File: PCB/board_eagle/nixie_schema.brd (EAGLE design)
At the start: 150 x 170 mm, 103 parts, among them P1 100k, Q1 BC856B, Q2 IRF740S, U2 MC7940N

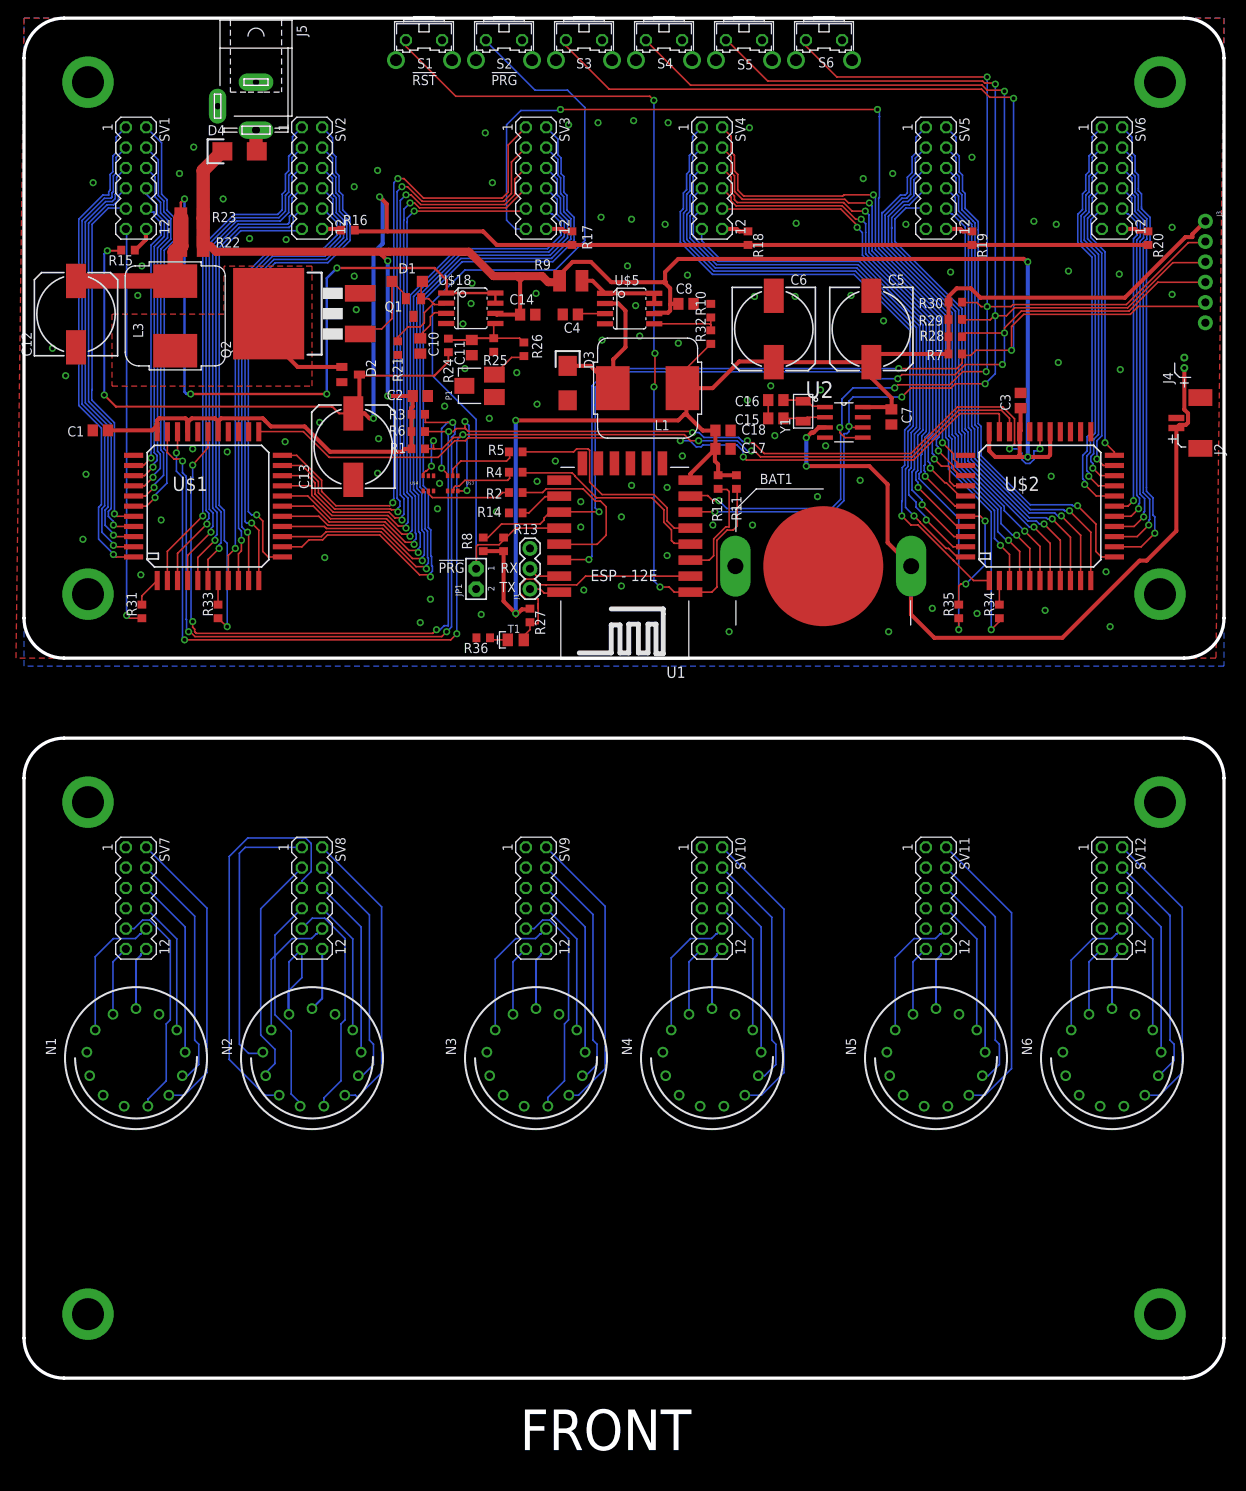
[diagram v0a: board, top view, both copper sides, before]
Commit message: Started fixing nixie tube footprint
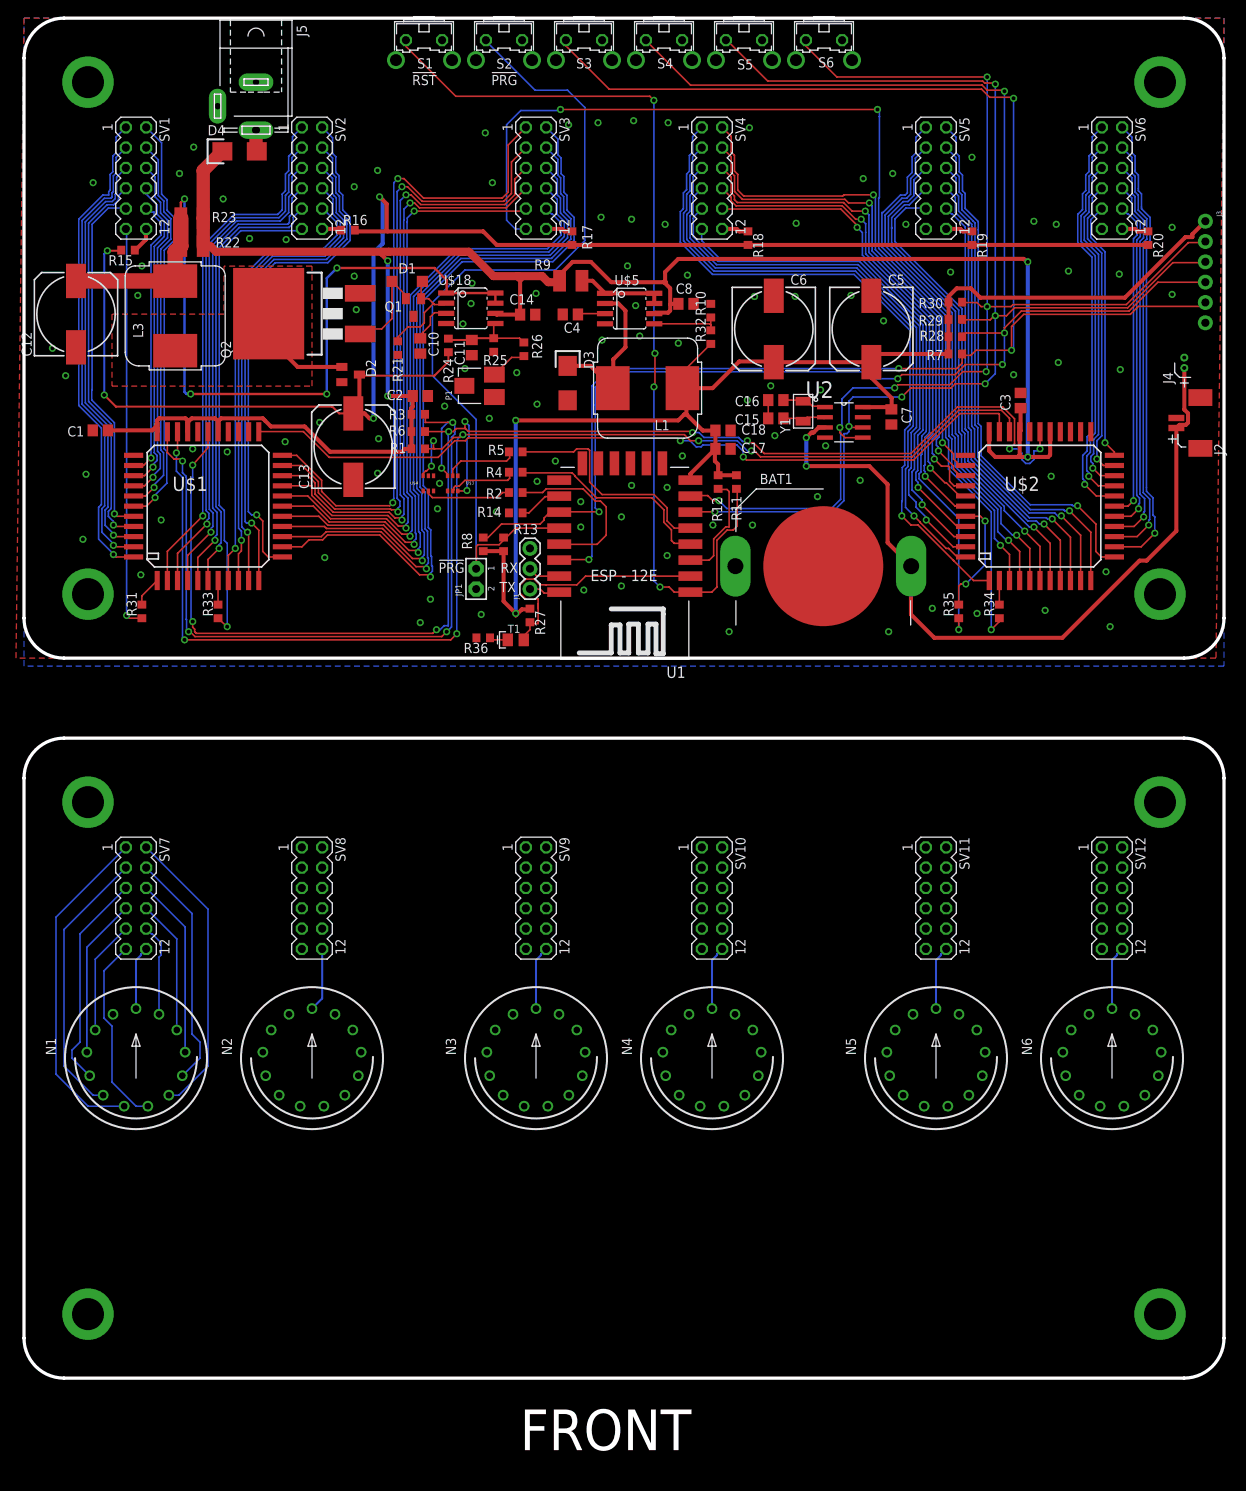
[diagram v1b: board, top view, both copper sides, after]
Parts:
- N1, N2, N3, N4, N5, N6: value IN-14 -> IN-14_FIXED
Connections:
- removed net N$101: N3.LHDP, SV9.11
- removed net N$102: N4.LHDP, SV10.11
- removed net N$104: N6.LHDP, SV12.11
- removed net N$105: N5.LHDP, SV11.11
- removed net N$31: N1.7, SV7.5
- removed net N$32: N1.8, SV7.3
- removed net N$33: N1.9, SV7.1
- removed net N$34: N2.9, SV8.1
- removed net N$35: N2.0, SV8.10
- removed net N$36: N2.1, SV8.8
- removed net N$37: N2.2, SV8.6
- removed net N$38: N2.3, SV8.4
- removed net N$39: N2.4, SV8.2
- removed net N$40: N2.5, SV8.9
- removed net N$41: N2.8, SV8.3
- removed net N$42: N2.7, SV8.5
- removed net N$43: N2.6, SV8.7
- removed net N$44: N4.1, SV10.8
- removed net N$46: N3.5, SV9.9
- removed net N$47: N3.6, SV9.7
- removed net N$48: N3.7, SV9.5
- removed net N$49: N3.8, SV9.3
- removed net N$50: N3.9, SV9.1
- removed net N$51: N3.0, SV9.10
- removed net N$52: N3.1, SV9.8
- removed net N$53: N3.2, SV9.6
- removed net N$54: N3.3, SV9.4
- removed net N$55: N3.4, SV9.2
- removed net N$56: N4.2, SV10.6
- removed net N$57: N4.3, SV10.4
- removed net N$58: N4.4, SV10.2
- removed net N$59: N4.5, SV10.9
- removed net N$60: N4.6, SV10.7
- removed net N$61: N4.7, SV10.5
- removed net N$62: N4.8, SV10.3
- removed net N$63: N4.9, SV10.1
- removed net N$64: N5.0, SV11.10
- removed net N$65: N5.1, SV11.8
- removed net N$66: N5.2, SV11.6
- removed net N$67: N5.3, SV11.4
- removed net N$68: N5.4, SV11.2
- removed net N$69: N5.5, SV11.9
- removed net N$70: N5.9, SV11.1
- removed net N$71: N5.8, SV11.3
- removed net N$72: N5.7, SV11.5
- removed net N$73: N5.6, SV11.7
- removed net N$75: N6.5, SV12.9
- removed net N$76: N6.6, SV12.7
- removed net N$77: N6.7, SV12.5
- removed net N$78: N6.8, SV12.3
- removed net N$79: N6.9, SV12.1
- removed net N$80: N6.0, SV12.10
- removed net N$81: N6.1, SV12.8
- removed net N$82: N6.2, SV12.6
- removed net N$83: N6.3, SV12.4
- removed net N$84: N6.4, SV12.2
- removed net N$86: N2.LHDP, SV8.11
- new net N$1: N2.RHDP, SV8.10
- new net N$2: N1.0, SV7.8
- new net N$6: N1.9, SV7.6
- new net N$7: N1.8, SV7.4
- net N$23: now also N3.RHDP, SV9.10; no longer N4.0, SV10.10
- net N$24: now also N1.7, SV7.2; no longer N1.0, SV7.10
- net N$25: now also SV7.9; no longer SV7.8
- net N$26: now also SV7.7; no longer SV7.6
- net N$27: now also SV7.5; no longer SV7.4
- net N$28: now also SV7.3; no longer SV7.2
- net N$29: now also SV7.1; no longer SV7.9
- net N$30: now also SV7.11; no longer SV7.7
- net N$94: now also N1.RHDP, SV7.10; no longer N1.LHDP, SV7.11
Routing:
- net N$42: track 51.0 -> 0.00 mm
- net N$68: track 37.8 -> 0.00 mm
- net N$58: track 37.4 -> 0.00 mm
- net N$39: track 37.2 -> 0.00 mm
- net N$84: track 37.1 -> 0.00 mm
- net N$55: track 36.6 -> 0.00 mm
- net N$34: track 35.5 -> 0.00 mm
- net N$57: track 30.2 -> 0.00 mm
- net N$67: track 30.1 -> 0.00 mm
- net N$38: track 29.7 -> 0.00 mm
- net N$7: track 0.00 -> 29.7 mm
- net N$83: track 29.7 -> 0.00 mm
- net N$54: track 29.7 -> 0.00 mm
- net N$41: track 29.3 -> 0.00 mm
- net N$40: track 29.0 -> 0.00 mm
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
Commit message: Top board touting complete
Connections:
- new net N$31: N2.7, SV8.4
- new net N$32: N2.8, SV8.6
- new net N$33: N2.9, SV8.8
- new net N$34: N2.0, SV8.10
- new net N$35: N3.RHDP, SV9.11
- new net N$36: N3.6, SV9.2
- new net N$37: N3.7, SV9.4
- new net N$38: N2.5, SV8.1
- new net N$39: N2.4, SV8.3
- new net N$40: N2.3, SV8.5
- new net N$41: N2.2, SV8.7
- new net N$42: N2.1, SV8.9
- new net N$43: N3.8, SV9.6
- new net N$44: N3.9, SV9.8
- new net N$46: N3.0, SV9.10
- new net N$47: N4.RHDP, SV10.11
- new net N$48: N4.6, SV10.2
- new net N$49: N3.5, SV9.1
- new net N$50: N3.4, SV9.3
- new net N$51: N3.3, SV9.5
- new net N$52: N3.2, SV9.7
- new net N$53: N3.1, SV9.9
- new net N$54: N4.7, SV10.4
- new net N$55: N4.8, SV10.6
- new net N$56: N4.9, SV10.8
- new net N$57: N4.0, SV10.10
- new net N$58: N5.RHDP, SV11.11
- new net N$59: N4.5, SV10.1
- new net N$60: N4.4, SV10.3
- new net N$61: N4.3, SV10.5
- new net N$62: N4.2, SV10.7
- new net N$63: N4.1, SV10.9
- new net N$64: N5.6, SV11.2
- new net N$65: N5.7, SV11.4
- new net N$66: N5.8, SV11.6
- new net N$67: N5.9, SV11.8
- new net N$68: N5.0, SV11.10
- new net N$69: N5.5, SV11.1
- new net N$70: N5.4, SV11.3
- new net N$71: N5.3, SV11.5
- new net N$72: N5.2, SV11.7
- new net N$73: N5.1, SV11.9
- new net N$75: N6.RHDP, SV12.11
- new net N$76: N6.6, SV12.2
- new net N$77: N6.7, SV12.4
- new net N$78: N6.8, SV12.6
- new net N$79: N6.9, SV12.8
- new net N$80: N6.5, SV12.1
- new net N$81: N6.4, SV12.3
- new net N$82: N6.3, SV12.5
- new net N$83: N6.2, SV12.7
- new net N$84: N6.1, SV12.9
- new net N$86: N6.0, SV12.10
- net HV_HA_1: now also SV1.9, U$1.40; no longer SV1.8, U$1.36
- net HV_HA_2: now also SV1.7, U$1.41; no longer SV1.6, U$1.37
- net HV_HA_3: now also SV1.5, U$1.42; no longer SV1.4, U$1.38
- net HV_HA_4: now also SV1.3, U$1.43; no longer SV1.2, U$1.39
- net HV_HA_5: now also SV1.1, U$1.44; no longer SV1.9, U$1.40
- net HV_HA_6: now also SV1.2, U$1.39; no longer SV1.7, U$1.41
- net HV_HA_7: now also SV1.4, U$1.38; no longer SV1.5, U$1.42
- net HV_HA_8: now also SV1.6, U$1.37; no longer SV1.3, U$1.43
- net HV_HA_9: now also SV1.8, U$1.36; no longer SV1.1, U$1.44
- net HV_HB_1: now also SV2.9, U$1.6; no longer SV2.8, U$1.9
- net HV_HB_2: now also SV2.7, U$1.5; no longer SV2.6, U$1.10
- net HV_HB_3: now also SV2.5, U$1.4; no longer SV2.4, U$1.11
- net HV_HB_4: now also SV2.3, U$1.3; no longer SV2.2, U$1.12
- net HV_HB_5: now also SV2.1, U$1.2; no longer SV2.9, U$1.6
- net HV_HB_6: now also SV2.2, U$1.12; no longer SV2.7, U$1.5
- net HV_HB_7: now also SV2.4, U$1.11; no longer SV2.5, U$1.4
- net HV_HB_8: now also SV2.6, U$1.10; no longer SV2.3, U$1.3
- net HV_HB_9: now also SV2.8, U$1.9; no longer SV2.1, U$1.2
- net HV_MA_1: now also SV3.9, U$1.18; no longer SV3.8, U$1.16
- net HV_MA_2: now also SV3.7, U$1.19; no longer SV3.6, U$1.15
- net HV_MA_3: now also SV3.5, U$1.20; no longer SV3.4, U$1.14
- net HV_MA_4: now also SV3.3, U$1.21; no longer SV3.2, U$1.13
- net HV_MA_5: now also SV3.1, U$1.22; no longer SV3.9, U$1.18
- net HV_MA_6: now also SV3.2, U$1.13; no longer SV3.7, U$1.19
- net HV_MA_7: now also SV3.4, U$1.14; no longer SV3.5, U$1.20
- net HV_MA_8: now also SV3.6, U$1.15; no longer SV3.3, U$1.21
- net HV_MA_9: now also SV3.8, U$1.16; no longer SV3.1, U$1.22
- net HV_MB_1: now also SV4.9, U$2.41; no longer SV4.8, U$2.38
- net HV_MB_2: now also SV4.7, U$2.42; no longer SV4.6, U$2.37
- net HV_MB_3: now also SV4.5, U$2.43; no longer SV4.4, U$2.36
- net HV_MB_4: now also SV4.3, U$2.44; no longer SV4.2, U$2.35
- net HV_MB_5: now also SV4.1, U$2.1; no longer SV4.9, U$2.41
- net HV_MB_6: now also SV4.2, U$2.35; no longer SV4.7, U$2.42
- net HV_MB_7: now also SV4.4, U$2.36; no longer SV4.5, U$2.43
- net HV_MB_8: now also SV4.6, U$2.37; no longer SV4.3, U$2.44
- net HV_MB_9: now also SV4.8, U$2.38; no longer SV4.1, U$2.1
- net HV_SA_1: now also SV5.9, U$2.7; no longer SV5.8, U$2.9
- net HV_SA_2: now also SV5.7, U$2.6; no longer SV5.6, U$2.10
- net HV_SA_3: now also SV5.5, U$2.5; no longer SV5.4, U$2.11
- net HV_SA_4: now also SV5.3, U$2.4; no longer SV5.2, U$2.12
- net HV_SA_5: now also SV5.1, U$2.3; no longer SV5.9, U$2.7
- net HV_SA_6: now also SV5.2, U$2.12; no longer SV5.7, U$2.6
- net HV_SA_7: now also SV5.4, U$2.11; no longer SV5.5, U$2.5
- net HV_SA_8: now also SV5.6, U$2.10; no longer SV5.3, U$2.4
- net HV_SA_9: now also SV5.8, U$2.9; no longer SV5.1, U$2.3
- net HV_SB_1: now also SV6.9, U$2.22; no longer SV6.8, U$2.16
- net HV_SB_2: now also SV6.7, U$2.21; no longer SV6.6, U$2.15
- net HV_SB_3: now also SV6.5, U$2.20; no longer SV6.4, U$2.14
- net HV_SB_4: now also SV6.3, U$2.19; no longer SV6.2, U$2.13
- net HV_SB_5: now also SV6.1, U$2.18; no longer SV6.9, U$2.22
- net HV_SB_6: now also SV6.2, U$2.13; no longer SV6.7, U$2.21
- net HV_SB_7: now also SV6.4, U$2.14; no longer SV6.5, U$2.20
- net HV_SB_8: now also SV6.6, U$2.15; no longer SV6.3, U$2.19
- net HV_SB_9: now also SV6.8, U$2.16; no longer SV6.1, U$2.18
- net N$1: now also SV8.11; no longer SV8.10
- net N$2: now also N1.6, SV7.2; no longer N1.0, SV7.8
- net N$23: now also N2.6, SV8.2; no longer N3.RHDP, SV9.10
- net N$24: now also N1.9, SV7.8; no longer N1.7, SV7.2
- net N$30: now also N1.RHDP; no longer N1.6
- net N$6: now also N1.7, SV7.4; no longer N1.9, SV7.6
- net N$7: now also SV7.6; no longer SV7.4
- net N$94: now also N1.0; no longer N1.RHDP
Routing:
- net N$49: track 0.00 -> 42.7 mm
- net N$38: track 0.00 -> 42.7 mm
- net N$48: track 0.00 -> 42.2 mm
- net N$36: track 0.00 -> 42.2 mm
- net N$69: track 0.00 -> 42.1 mm
- net N$59: track 0.00 -> 42.1 mm
- net N$80: track 0.00 -> 42.1 mm
- net N$23: track 0.00 -> 42.1 mm
- net N$76: track 0.00 -> 41.9 mm
- net N$64: track 0.00 -> 41.8 mm
- net N$39: track 0.00 -> 35.0 mm
- net N$50: track 0.00 -> 35.0 mm
- net N$54: track 0.00 -> 34.5 mm
- net N$70: track 0.00 -> 34.4 mm
- net N$60: track 0.00 -> 34.4 mm
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
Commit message: Added some values to components in schematic
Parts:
- C15, C16: value (none) -> 6p
- D1: value (none) -> 1n4148
- R11, R12, R13, R14, R8: value (none) -> 10k
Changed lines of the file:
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@@
 <attribute name="VALUE" x="50.927" y="25.908" size="1.27" layer="27"/>
 </element>
-<element name="R11" library="resistor" package="R0603" value="" x="89.054" y="22.014" smashed="yes" rot="R90">
+<element name="R11" library="resistor" package="R0603" value="10k" x="89.054" y="22.014" smashed="yes" rot="R90">
 <attribute name="NAME" x="89.689" y="17.188" size="1.27" layer="25" rot="R90"/>
 <attribute name="VALUE" x="90.959" y="21.379" size="1.27" layer="27" rot="R90"/>
 </element>
-<element name="R12" library="resistor" package="R0603" value="" x="86.768" y="22.014" smashed="yes" rot="R90">
+<element name="R12" library="resistor" package="R0603" value="10k" x="86.768" y="22.014" smashed="yes" rot="R90">
 <attribute name="NAME" x="87.276" y="17.061" size="1.27" layer="25" rot="R90"/>
 <attribute name="VALUE" x="88.673" y="21.379" size="1.27" layer="27" rot="R90"/>
 </element>
-<element name="R13" library="resistor" package="R0603" value="" x="59.944" y="14.224" smashed="yes" rot="R90">
+<element name="R13" library="resistor" package="R0603" value="10k" x="59.944" y="14.224" smashed="yes" rot="R90">
 <attribute name="NAME" x="64.262" y="16.764" size="1.27" layer="25" rot="R180"/>
 <attribute name="VALUE" x="61.849" y="13.589" size="1.27" layer="27" rot="R90"/>
 </element>
-<element name="R14" library="resistor" package="R0603" value="" x="61.468" y="18.161" smashed="yes">
+<element name="R14" library="resistor" package="R0603" value="10k" x="61.468" y="18.161" smashed="yes">
 <attribute name="NAME" x="56.642" y="17.653" size="1.27" layer="25"/>
 <attribute name="VALUE" x="60.833" y="16.256" size="1.27" layer="27"/>
@@
 <attribute name="VALUE" x="23.54" y="58.175" size="1.27" layer="27" rot="R180"/>
 </element>
-<element name="D1" library="diode" package="SOD123" value="" x="47.9" y="47.09"/>
+<element name="D1" library="diode" package="SOD123" value="1n4148" x="47.9" y="47.09"/>
 <element name="R24" library="resistor" package="R0603" value="330k" x="53.046" y="39.09" smashed="yes" rot="R90">
 <attribute name="NAME" x="53.681" y="34.391" size="1.27" layer="25" rot="R90"/>
@@
 <attribute name="VCC" value="1.8-5.5V" x="102.484" y="29.474" size="1.778" layer="27" display="off"/>
 </element>
-<element name="C15" library="rcl" package="C0805" value="" x="93.98" y="29.972" smashed="yes" rot="R180">
+<element name="C15" library="rcl" package="C0805" value="6p" x="93.98" y="29.972" smashed="yes" rot="R180">
 <attribute name="NAME" x="91.948" y="30.48" size="1.27" layer="25" rot="R180"/>
 <attribute name="VALUE" x="95.25" y="32.512" size="1.27" layer="27" rot="R180"/>
 </element>
-<element name="C16" library="rcl" package="C0805" value="" x="93.98" y="32.258" smashed="yes" rot="R180">
+<element name="C16" library="rcl" package="C0805" value="6p" x="93.98" y="32.258" smashed="yes" rot="R180">
 <attribute name="NAME" x="91.948" y="32.766" size="1.27" layer="25" rot="R180"/>
 <attribute name="VALUE" x="95.25" y="34.798" size="1.27" layer="27" rot="R180"/>
@@
 <attribute name="VALUE" x="84.963" y="29.845" size="1.27" layer="27"/>
 </element>
-<element name="R8" library="resistor" package="R0603" value="" x="57.404" y="14.224" smashed="yes" rot="R90">
+<element name="R8" library="resistor" package="R0603" value="10k" x="57.404" y="14.224" smashed="yes" rot="R90">
 <attribute name="NAME" x="56.007" y="13.589" size="1.27" layer="25" rot="R90"/>
 <attribute name="VALUE" x="59.309" y="13.589" size="1.27" layer="27" rot="R90"/>
